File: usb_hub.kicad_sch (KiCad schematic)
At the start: 133 parts, among them J5 USB-C_Kycon_KUSBX-SL2-CS1N24-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, J6 USB-C_Kycon_KUSBX-SL2-CS1N24-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, Q21 DMC2400UV-7, Q26 DMC2400UV-7, Q27 DMC2400UV-7, Q29 DMC2400UV-7, U17 TPD4E05U06QDQARQ1, U18 AP22615A_TSOT26, U19 TPD4E05U06QDQARQ1, U20 AP22615A_TSOT26, U21 USB7252C, U24 TPD4E05U06QDQARQ1, U25 TPD4E05U06QDQARQ1, U27 TPD4E05U06QDQARQ1, U28 TPD4E05U06QDQARQ1, U52 SST26VF064B, Y2 Oscillator_25MHz_ESC_2016MV

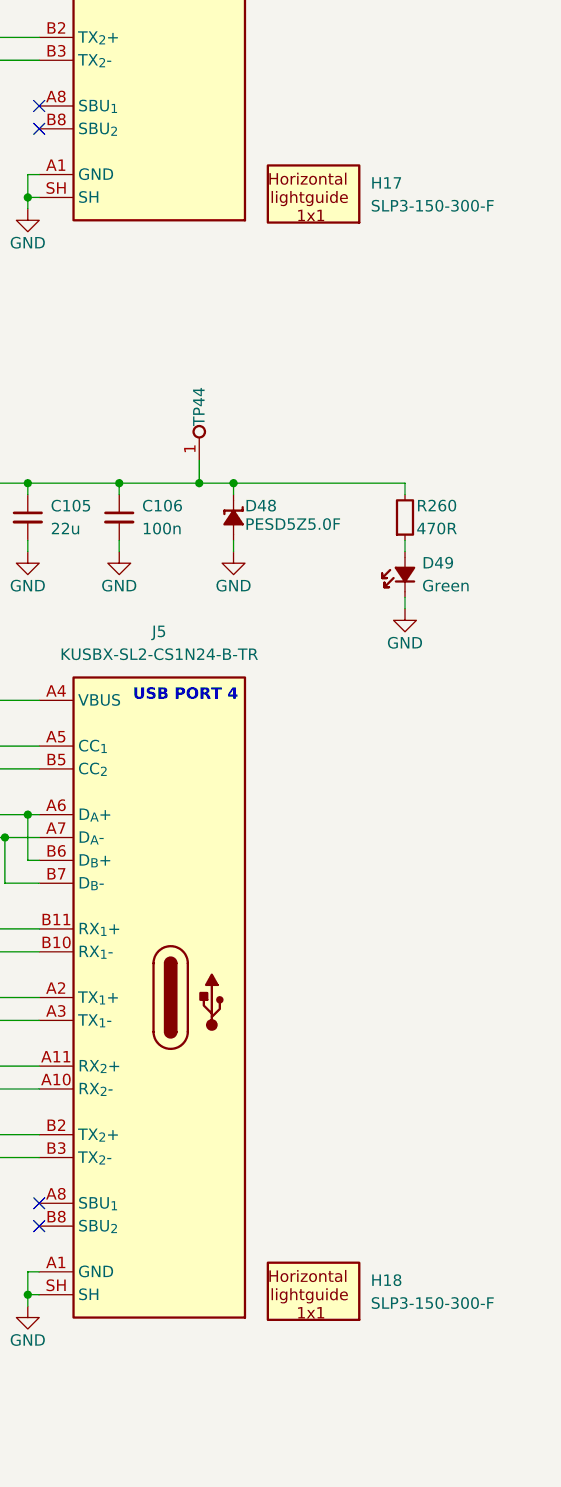
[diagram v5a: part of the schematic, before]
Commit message: [#89536] Replace lightpipes with 1271.1001 model, place them in correct positions on PCB
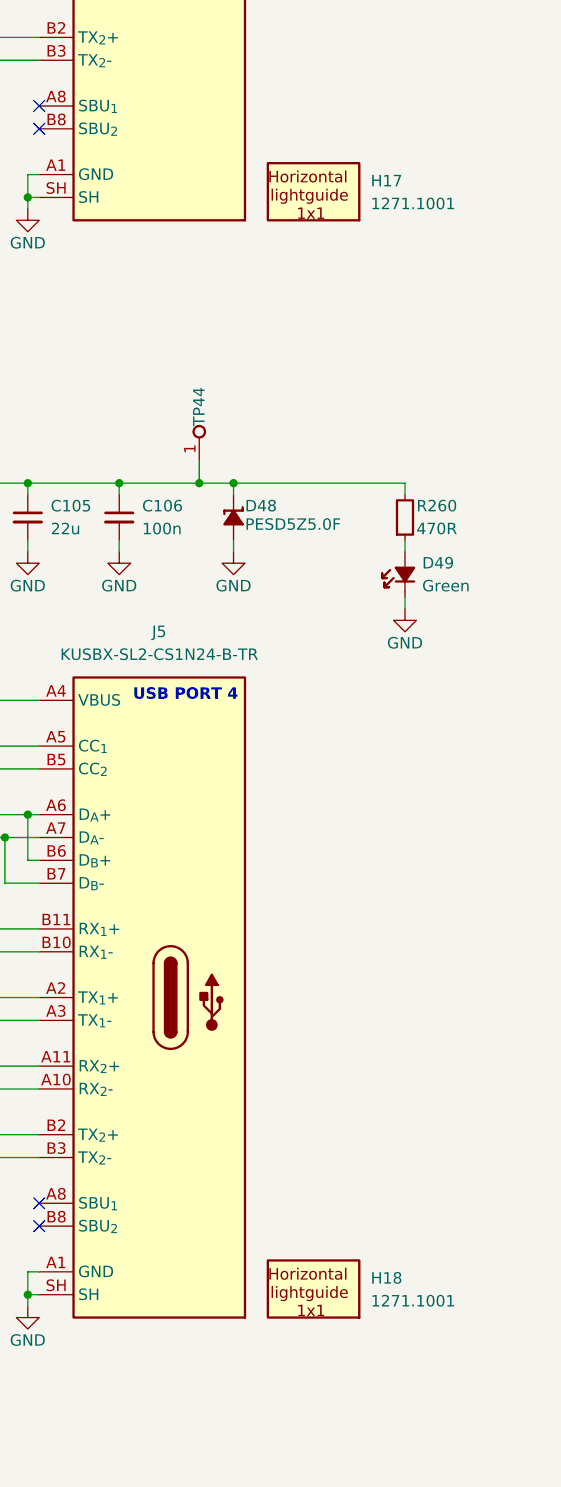
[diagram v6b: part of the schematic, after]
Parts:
- H17, H18: value Lightpipe_Bivar_SLP3-150-300-F -> Lightpipe_Mentor_1271.1001; footprint antmicro-footprints:Mech_Lightpipe_Bivar_SLP3-150-300-F -> antmicro-footprints:Mech_Lightpipe_Mentor_1271.1001; symbol antmicroMechanicalParts:Lightpipe_Bivar_SLP3-150-300-F -> antmicroMechanicalParts:Lightpipe_Mentor_1271.1001; MPN SLP3-150-300-F -> 1271.1001; Manufacturer BIVAR -> Mentor Worldwide
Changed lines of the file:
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@@
 	)
 	(symbol
-		(lib_id "antmicroMechanicalParts:Lightpipe_Bivar_SLP3-150-300-F")
+		(lib_id "antmicroMechanicalParts:Lightpipe_Mentor_1271.1001")
 		(at 382.27 121.92 0)
 		(unit 1)
@@
 		(fields_autoplaced yes)
 		(property "Reference" "H17"
-			(at 388.62 120.3517 0)
+			(at 388.62 120.0977 0)
 			(effects
 				(font
@@
 			)
 		)
-		(property "Value" "Lightpipe_Bivar_SLP3-150-300-F"
-			(at 394.03 129.235 0)
-			(effects
-				(font
-					(size 1.27 1.27)
-					(thickness 0.15)
-				)
-				(justify left bottom)
-				(hide yes)
-			)
-		)
-		(property "Footprint" "antmicro-footprints:Mech_Lightpipe_Bivar_SLP3-150-300-F"
-			(at 394.03 131.775 0)
-			(effects
-				(font
-					(size 1.27 1.27)
-					(thickness 0.15)
-				)
-				(justify left bottom)
-				(hide yes)
-			)
-		)
-		(property "Datasheet" "https://eu.mouser.com/datasheet/2/50/Bivar_SLP3_150_XXX_X_N-3318840.pdf"
-			(at 394.03 134.315 0)
-			(effects
-				(font
-					(size 1.27 1.27)
-					(thickness 0.15)
-				)
-				(justify left bottom)
-				(hide yes)
-			)
-		)
-		(property "Description" "LED Light Pipe, Rigid Board, Horizontal"
-			(at 394.03 144.475 0)
-			(effects
-				(font
-					(size 1.27 1.27)
-				)
-				(justify left bottom)
-				(hide yes)
-			)
-		)
-		(property "Manufacturer" "BIVAR"
-			(at 394.03 136.855 0)
-			(effects
-				(font
-					(size 1.27 1.27)
-					(thickness 0.15)
-				)
-				(justify left bottom)
-				(hide yes)
-			)
-		)
-		(property "MPN" "SLP3-150-300-F"
-			(at 388.62 122.8917 0)
+		(property "Value" "Lightpipe_Mentor_1271.1001"
+			(at 402.59 129.54 0)
+			(effects
+				(font
+					(size 1.27 1.27)
+					(thickness 0.15)
+				)
+				(justify left bottom)
+				(hide yes)
+			)
+		)
+		(property "Footprint" "antmicro-footprints:Mech_Lightpipe_Mentor_1271.1001"
+			(at 402.59 132.08 0)
+			(effects
+				(font
+					(size 1.27 1.27)
+					(thickness 0.15)
+				)
+				(justify left bottom)
+				(hide yes)
+			)
+		)
+		(property "Datasheet" "https://www.mentor.de.com/productpdfs/ll/ll14-20.pdf"
+			(at 402.59 134.62 0)
+			(effects
+				(font
+					(size 1.27 1.27)
+					(thickness 0.15)
+				)
+				(justify left bottom)
+				(hide yes)
+			)
+		)
+		(property "Description" "Light Pipe, 14.45 mm, 1 Pipe, Circular, PC Board, Transparent"
+			(at 402.59 144.78 0)
+			(effects
+				(font
+					(size 1.27 1.27)
+				)
+				(justify left bottom)
+				(hide yes)
+			)
+		)
+		(property "Manufacturer" "Mentor Worldwide"
+			(at 402.59 137.16 0)
+			(effects
+				(font
+					(size 1.27 1.27)
+					(thickness 0.15)
+				)
+				(justify left bottom)
+				(hide yes)
+			)
+		)
+		(property "MPN" "1271.1001"
+			(at 388.62 122.6377 0)
 			(effects
 				(font
@@
 		)
 		(property "Author" "Antmicro"
-			(at 394.03 139.395 0)
+			(at 402.59 139.7 0)
 			(effects
 				(font
@@
 		)
 		(property "License" "Apache-2.0"
-			(at 394.03 141.935 0)
+			(at 402.59 142.24 0)
 			(effects
 				(font
@@
 	)
 	(symbol
-		(lib_id "antmicroMechanicalParts:Lightpipe_Bivar_SLP3-150-300-F")
+		(lib_id "antmicroMechanicalParts:Lightpipe_Mentor_1271.1001")
 		(at 382.27 243.84 0)
 		(unit 1)
@@
 		(fields_autoplaced yes)
 		(property "Reference" "H18"
-			(at 388.62 242.2717 0)
+			(at 388.62 242.0177 0)
 			(effects
 				(font
@@
 			)
 		)
-		(property "Value" "Lightpipe_Bivar_SLP3-150-300-F"
-			(at 394.03 251.155 0)
-			(effects
-				(font
-					(size 1.27 1.27)
-					(thickness 0.15)
-				)
-				(justify left bottom)
-				(hide yes)
-			)
-		)
-		(property "Footprint" "antmicro-footprints:Mech_Lightpipe_Bivar_SLP3-150-300-F"
-			(at 394.03 253.695 0)
-			(effects
-				(font
-					(size 1.27 1.27)
-					(thickness 0.15)
-				)
-				(justify left bottom)
-				(hide yes)
-			)
-		)
-		(property "Datasheet" "https://eu.mouser.com/datasheet/2/50/Bivar_SLP3_150_XXX_X_N-3318840.pdf"
-			(at 394.03 256.235 0)
-			(effects
-				(font
-					(size 1.27 1.27)
-					(thickness 0.15)
-				)
-				(justify left bottom)
-				(hide yes)
-			)
-		)
-		(property "Description" "LED Light Pipe, Rigid Board, Horizontal"
-			(at 394.03 266.395 0)
-			(effects
-				(font
-					(size 1.27 1.27)
-				)
-				(justify left bottom)
-				(hide yes)
-			)
-		)
-		(property "Manufacturer" "BIVAR"
-			(at 394.03 258.775 0)
-			(effects
-				(font
-					(size 1.27 1.27)
-					(thickness 0.15)
-				)
-				(justify left bottom)
-				(hide yes)
-			)
-		)
-		(property "MPN" "SLP3-150-300-F"
-			(at 388.62 244.8117 0)
+		(property "Value" "Lightpipe_Mentor_1271.1001"
+			(at 402.59 251.46 0)
+			(effects
+				(font
+					(size 1.27 1.27)
+					(thickness 0.15)
+				)
+				(justify left bottom)
+				(hide yes)
+			)
+		)
+		(property "Footprint" "antmicro-footprints:Mech_Lightpipe_Mentor_1271.1001"
+			(at 402.59 254 0)
+			(effects
+				(font
+					(size 1.27 1.27)
+					(thickness 0.15)
+				)
+				(justify left bottom)
+				(hide yes)
+			)
+		)
+		(property "Datasheet" "https://www.mentor.de.com/productpdfs/ll/ll14-20.pdf"
+			(at 402.59 256.54 0)
+			(effects
+				(font
+					(size 1.27 1.27)
+					(thickness 0.15)
+				)
+				(justify left bottom)
+				(hide yes)
+			)
+		)
+		(property "Description" "Light Pipe, 14.45 mm, 1 Pipe, Circular, PC Board, Transparent"
+			(at 402.59 266.7 0)
+			(effects
+				(font
+					(size 1.27 1.27)
+				)
+				(justify left bottom)
+				(hide yes)
+			)
+		)
+		(property "Manufacturer" "Mentor Worldwide"
+			(at 402.59 259.08 0)
+			(effects
+				(font
+					(size 1.27 1.27)
+					(thickness 0.15)
+				)
+				(justify left bottom)
+				(hide yes)
+			)
+		)
+		(property "MPN" "1271.1001"
+			(at 388.62 244.5577 0)
 			(effects
 				(font
@@
 		)
 		(property "Author" "Antmicro"
-			(at 394.03 261.315 0)
+			(at 402.59 261.62 0)
 			(effects
 				(font
@@
 		)
 		(property "License" "Apache-2.0"
-			(at 394.03 263.855 0)
-			(effects
-				(font
+			(at 402.59 264.16 0)
+			(effects
+				(font

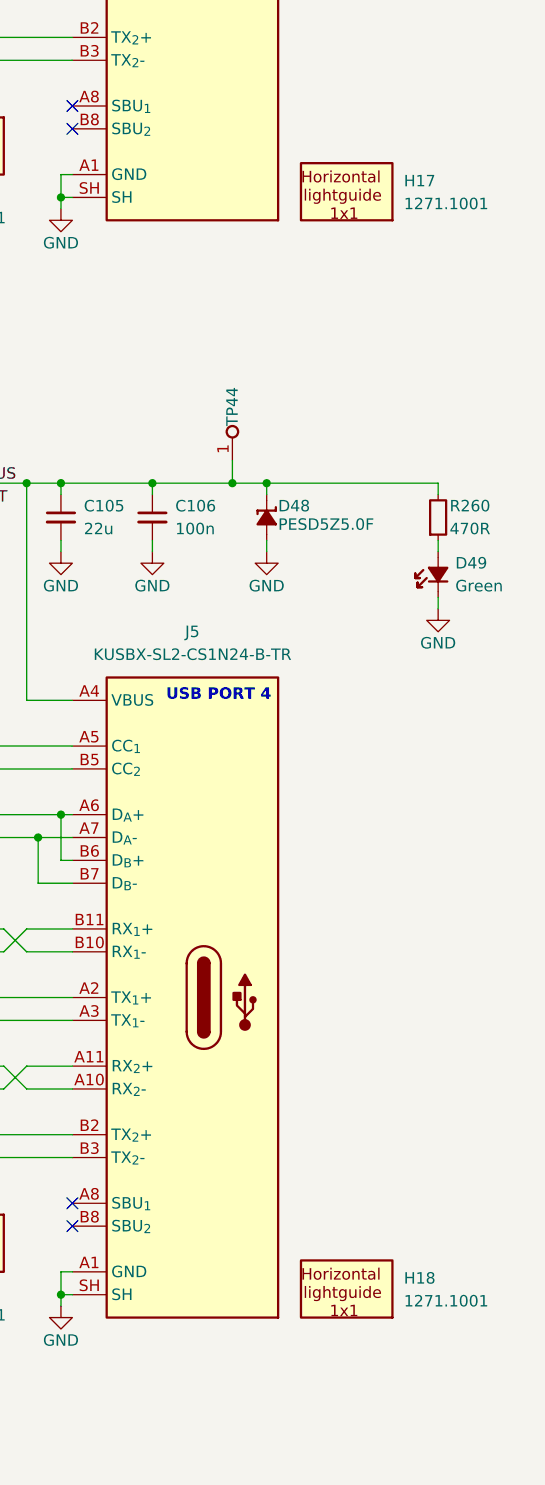
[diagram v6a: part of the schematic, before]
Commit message: [#89536] Remove lighpipes footprints
Front panel mounted will be used
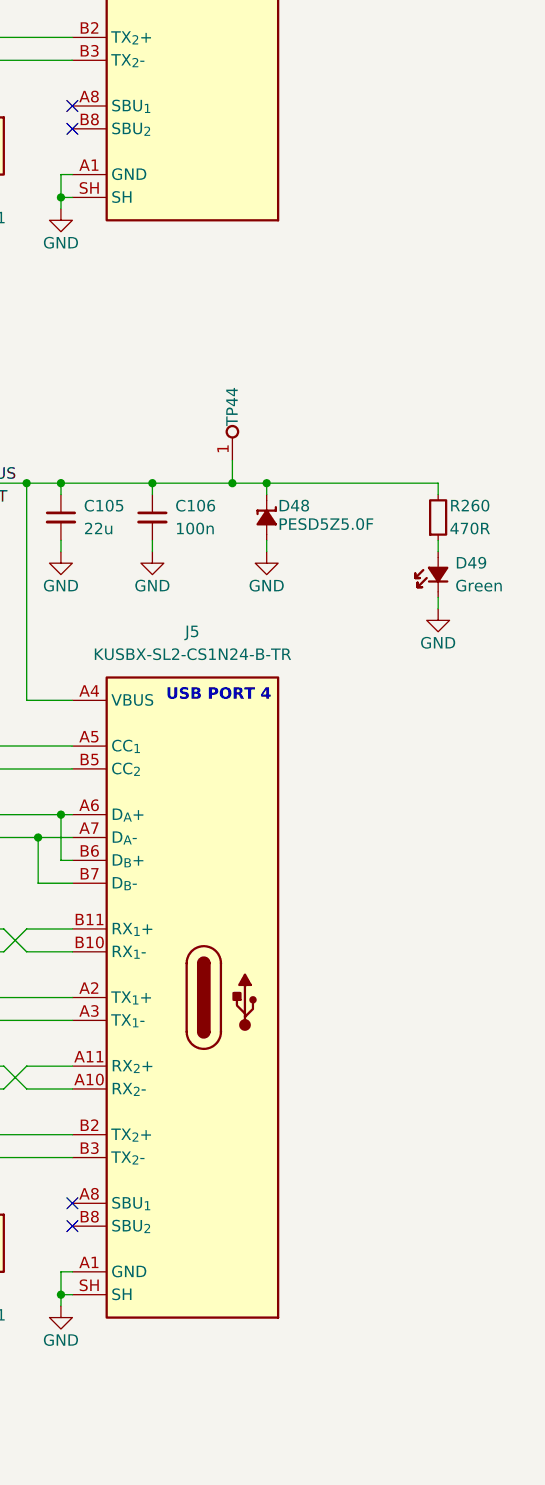
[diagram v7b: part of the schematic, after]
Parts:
- removed H17, H18: Lightpipe_Mentor_1271.1001, antmicro-footprints:Mech_Lightpipe_Mentor_1271.1001, symbol antmicroMechanicalParts:Lightpipe_Mentor_1271.1001
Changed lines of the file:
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@@
-	)
-	(symbol
-		(lib_id "antmicroMechanicalParts:Lightpipe_Mentor_1271.1001")
-		(at 382.27 121.92 0)
-		(unit 1)
-		(exclude_from_sim no)
-		(in_bom yes)
-		(on_board yes)
-		(dnp no)
-		(fields_autoplaced yes)
-		(property "Reference" "H17"
-			(at 388.62 120.0977 0)
-			(effects
-				(font
-					(size 1.27 1.27)
-					(thickness 0.15)
-				)
-				(justify left)
-			)
-		)
-		(property "Value" "Lightpipe_Mentor_1271.1001"
-			(at 402.59 129.54 0)
-			(effects
-				(font
-					(size 1.27 1.27)
-					(thickness 0.15)
-				)
-				(justify left bottom)
-				(hide yes)
-			)
-		)
-		(property "Footprint" "antmicro-footprints:Mech_Lightpipe_Mentor_1271.1001"
-			(at 402.59 132.08 0)
-			(effects
-				(font
-					(size 1.27 1.27)
-					(thickness 0.15)
-				)
-				(justify left bottom)
-				(hide yes)
-			)
-		)
-		(property "Datasheet" "https://www.mentor.de.com/productpdfs/ll/ll14-20.pdf"
-			(at 402.59 134.62 0)
-			(effects
-				(font
-					(size 1.27 1.27)
-					(thickness 0.15)
-				)
-				(justify left bottom)
-				(hide yes)
-			)
-		)
-		(property "Description" "Light Pipe, 14.45 mm, 1 Pipe, Circular, PC Board, Transparent"
-			(at 402.59 144.78 0)
-			(effects
-				(font
-					(size 1.27 1.27)
-				)
-				(justify left bottom)
-				(hide yes)
-			)
-		)
-		(property "Manufacturer" "Mentor Worldwide"
-			(at 402.59 137.16 0)
-			(effects
-				(font
-					(size 1.27 1.27)
-					(thickness 0.15)
-				)
-				(justify left bottom)
-				(hide yes)
-			)
-		)
-		(property "MPN" "1271.1001"
-			(at 388.62 122.6377 0)
-			(effects
-				(font
-					(size 1.27 1.27)
-					(thickness 0.15)
-				)
-				(justify left)
-			)
-		)
-		(property "Author" "Antmicro"
-			(at 402.59 139.7 0)
-			(effects
-				(font
-					(size 1.27 1.27)
-					(thickness 0.15)
-				)
-				(justify left bottom)
-				(hide yes)
-			)
-		)
-		(property "License" "Apache-2.0"
-			(at 402.59 142.24 0)
-			(effects
-				(font
-					(size 1.27 1.27)
-					(thickness 0.15)
-				)
-				(justify left bottom)
-				(hide yes)
-			)
-		)
-		(instances
-			(project "jetson-agx-thor-baseboard"
-				(path "/f569b0be-0afd-48b7-93ee-28582a4c645c/3fd0fbfa-9a42-4c7b-8c1c-08c3e88df372"
-					(reference "H17")
-					(unit 1)
-				)
-			)
-		)
 	)
 	(symbol
@@
 					(unit 1)
 				)
-			)
-		)
-	)
-	(symbol
-		(lib_id "antmicroMechanicalParts:Lightpipe_Mentor_1271.1001")
-		(at 382.27 243.84 0)
-		(unit 1)
-		(exclude_from_sim no)
-		(in_bom yes)
-		(on_board yes)
-		(dnp no)
-		(fields_autoplaced yes)
-		(property "Reference" "H18"
-			(at 388.62 242.0177 0)
-			(effects
-				(font
-					(size 1.27 1.27)
-					(thickness 0.15)
-				)
-				(justify left)
-			)
-		)
-		(property "Value" "Lightpipe_Mentor_1271.1001"
-			(at 402.59 251.46 0)
-			(effects
-				(font
-					(size 1.27 1.27)
-					(thickness 0.15)
-				)
-				(justify left bottom)
-				(hide yes)
-			)
-		)
-		(property "Footprint" "antmicro-footprints:Mech_Lightpipe_Mentor_1271.1001"
-			(at 402.59 254 0)
-			(effects
-				(font
-					(size 1.27 1.27)
-					(thickness 0.15)
-				)
-				(justify left bottom)
-				(hide yes)
-			)
-		)
-		(property "Datasheet" "https://www.mentor.de.com/productpdfs/ll/ll14-20.pdf"
-			(at 402.59 256.54 0)
-			(effects
-				(font
-					(size 1.27 1.27)
-					(thickness 0.15)
-				)
-				(justify left bottom)
-				(hide yes)
-			)
-		)
-		(property "Description" "Light Pipe, 14.45 mm, 1 Pipe, Circular, PC Board, Transparent"
-			(at 402.59 266.7 0)
-			(effects
-				(font
-					(size 1.27 1.27)
-				)
-				(justify left bottom)
-				(hide yes)
-			)
-		)
-		(property "Manufacturer" "Mentor Worldwide"
-			(at 402.59 259.08 0)
-			(effects
-				(font
-					(size 1.27 1.27)
-					(thickness 0.15)
-				)
-				(justify left bottom)
-				(hide yes)
-			)
-		)
-		(property "MPN" "1271.1001"
-			(at 388.62 244.5577 0)
-			(effects
-				(font
-					(size 1.27 1.27)
-					(thickness 0.15)
-				)
-				(justify left)
-			)
-		)
-		(property "Author" "Antmicro"
-			(at 402.59 261.62 0)
-			(effects
-				(font
-					(size 1.27 1.27)
-					(thickness 0.15)
-				)
-				(justify left bottom)
-				(hide yes)
-			)
-		)
-		(property "License" "Apache-2.0"
-			(at 402.59 264.16 0)
-			(effects
-				(font
-					(size 1.27 1.27)
-					(thickness 0.15)
-				)
-				(justify left bottom)
-				(hide yes)
-			)
-		)
-		(instances
-			(project "jetson-agx-thor-baseboard"
-				(path "/f569b0be-0afd-48b7-93ee-28582a4c645c/3fd0fbfa-9a42-4c7b-8c1c-08c3e88df372"
-					(reference "H18")
-					(unit 1)
-				)
